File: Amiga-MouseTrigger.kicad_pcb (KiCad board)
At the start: 2 copper layers, 28.2 x 28.2 mm, 11 parts, among them J1 INPUT_SIGNALS, J2 OUTPUT, J3 POWER, J99 OSHW_LOGO, U1 74LS74

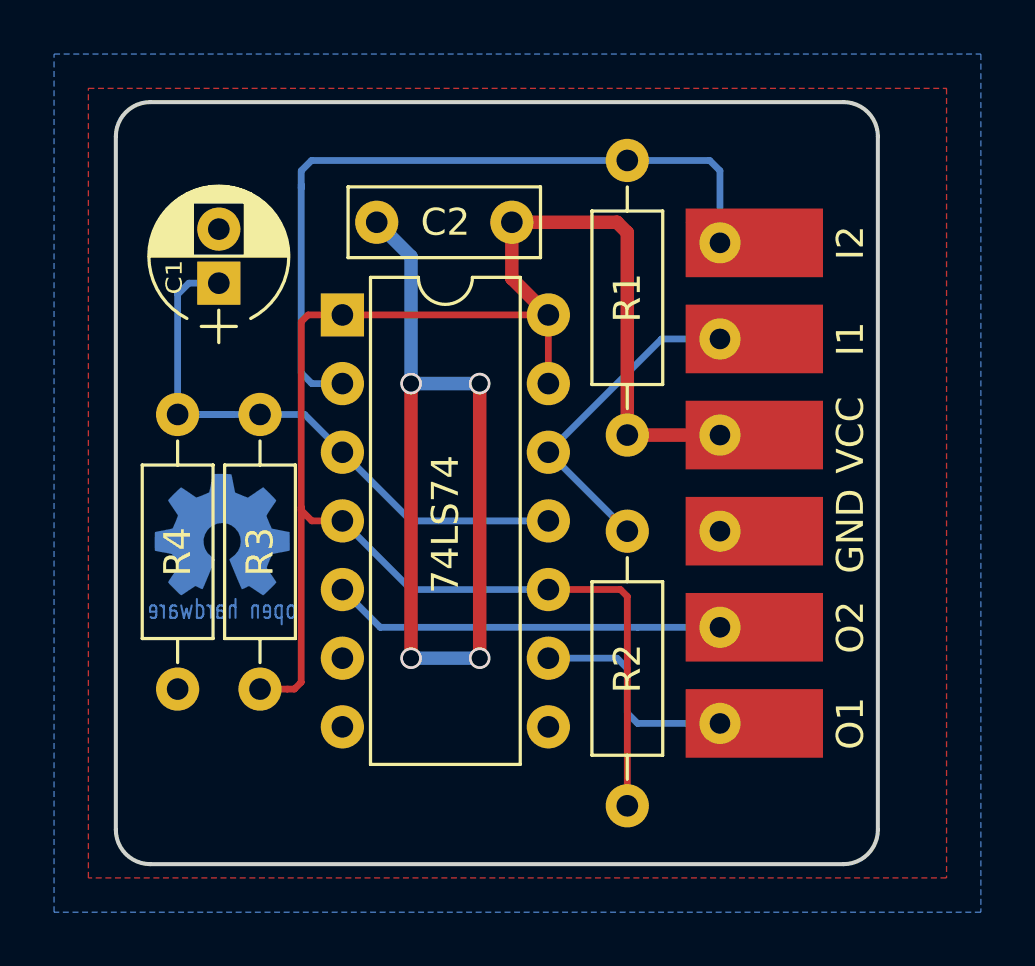
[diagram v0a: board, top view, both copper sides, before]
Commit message: Replace THT elements with SMD.
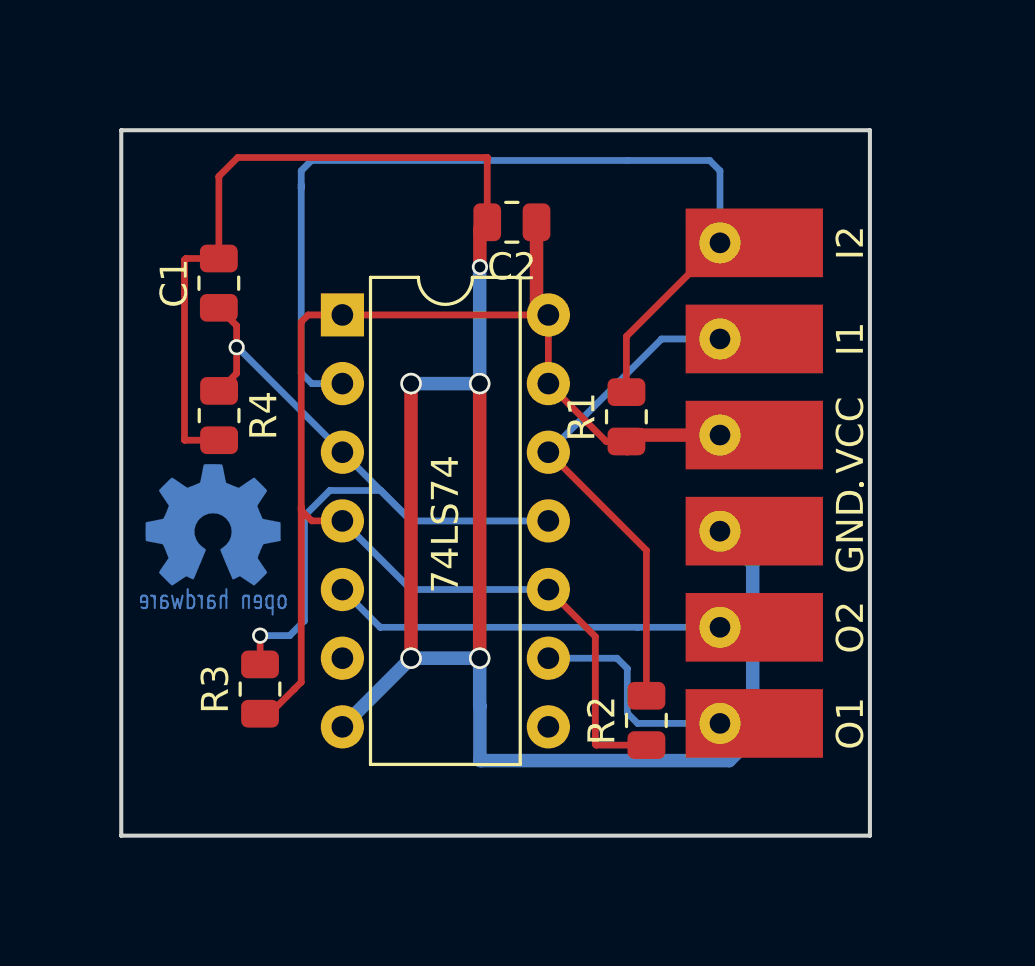
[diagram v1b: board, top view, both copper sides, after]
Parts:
- added G***: LOGO, Library:cyberkolo_logo_pcb, B.Cu at (126.0, 99.8)
- C1: footprint Capacitors_THT:CP_Radial_D5.0mm_P2.00mm -> Resistor_SMD:R_0805_2012Metric
- C2: footprint Capacitors_THT:C_Disc_D7.0mm_W2.5mm_P5.00mm -> Resistor_SMD:R_0805_2012Metric
- R1, R2, R3, R4: footprint Resistors_THT:R_Axial_DIN0207_L6.3mm_D2.5mm_P10.16mm_Horizontal -> Resistor_SMD:R_0805_2012Metric
- moved R2 3.24 mm to (141.3, 115.8)
- moved R4 1.53 mm to (125.5, 104.6)
- moved R1 0.68 mm to (140.6, 104.6)
- moved J99 0.49 mm to (125.3, 108.6)
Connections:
- U1 pad 6: (no net) -> unconnected-(U1A-~{Q}-Pad6)
- U1 pad 8: (no net) -> unconnected-(U1B-~{Q}-Pad8)
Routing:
- net GND: track 31.9 -> 82.4 mm, vias 4 -> 5
- net VCC: track 67.9 -> 57.5 mm
- net Net-(J1-Pin_1): track 28.8 -> 35.8 mm
- net Net-(U1A-Cp): track 23.3 -> 29.5 mm, vias 0 -> 2
- net Net-(J1-Pin_2): track 12.7 -> 18.6 mm
- removed copper zone on B.Cu, net GND
- removed copper zone on F.Cu, net GND
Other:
- board size 28.2 x 28.2 mm -> 27.7 x 26.1 mm
- net class Default removed
- net class Power removed
- board text added: "Cyberk0lo"
- board text added: "V3"
- board text added: "github.com/k0lo86/ Amiga-MouseTrigger"
- board text removed: "V2"
- board text removed: "github.com/SukkoPera/ OpenAmigaMouseTrigger"
